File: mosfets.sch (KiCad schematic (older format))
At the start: 72 parts, among them P5 HP_MOSFETS, P6 MP_MOSFETS, Q1 2N7002P, Q10 2N7002P, Q11 2N7002P, Q12 BC846BPDW1, Q13 BC846BPDW1, Q14 SI2318CDS-T1-GE3, Q15 IRFB7545PbF, Q16 2N7002P, Q17 2N7002P, Q18 BC846BPDW1, Q19 BC846BPDW1, Q2 2N7002P, Q20 SI2318CDS-T1-GE3, Q21 IRFB7545PbF, Q3 2N7002P, Q4 BC846BPDW1, Q5 BC846BPDW1, Q6 BC846BPDW1, Q7 IRFB7545PbF, Q8 SI2318CDS-T1-GE3, Q9 IRFB7545PbF

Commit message: fixed minor issue
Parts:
- Q15, Q21, Q7, Q9: footprint to:TO-220 -> to:TO-220-3
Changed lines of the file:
@@
 F 0 "Q9" H 3302 1935 34  0000 L CNN
 F 1 "IRFB7545PbF" H 3302 1866 34  0000 L CNN
-F 2 "to:TO-220" H 2925 1700 60  0001 C CNN
+F 2 "to:TO-220-3" H 2925 1700 60  0001 C CNN
 F 3 "" H 2925 1700 60  0000 C CNN
 	1    2925 1700
@@
 F 0 "Q21" H 8677 1935 34  0000 L CNN
 F 1 "IRFB7545PbF" H 8677 1866 34  0000 L CNN
-F 2 "to:TO-220" H 8300 1700 60  0001 C CNN
+F 2 "to:TO-220-3" H 8300 1700 60  0001 C CNN
 F 3 "" H 8300 1700 60  0000 C CNN
 	1    8300 1700
@@
 F 0 "Q7" H 3252 5835 34  0000 L CNN
 F 1 "IRFB7545PbF" H 3252 5766 34  0000 L CNN
-F 2 "to:TO-220" H 2875 5600 60  0001 C CNN
+F 2 "to:TO-220-3" H 2875 5600 60  0001 C CNN
 F 3 "" H 2875 5600 60  0000 C CNN
 	1    2875 5600
@@
 F 0 "Q15" H 6052 1935 34  0000 L CNN
 F 1 "IRFB7545PbF" H 6052 1866 34  0000 L CNN
-F 2 "to:TO-220" H 5675 1700 60  0001 C CNN
+F 2 "to:TO-220-3" H 5675 1700 60  0001 C CNN
 F 3 "" H 5675 1700 60  0000 C CNN
 	1    5675 1700

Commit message: fixed some errors
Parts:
- D11, D15, D7: footprint diodes:SOD-80C -> diodes:DO213AA_SOD-80_MiniMelf
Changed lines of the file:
@@
 F 0 "D7" V 3298 3047 34  0000 R CNN
 F 1 "1n4148" V 3229 3047 34  0000 R CNN
-F 2 "diodes:SOD-80C" H 3150 3075 60  0001 C CNN
+F 2 "diodes:DO213AA_SOD-80_MiniMelf" H 3150 3075 60  0001 C CNN
 F 3 "" H 3150 3075 60  0000 C CNN
 	1    3150 3075
@@
 F 0 "D11" V 6048 3047 34  0000 R CNN
 F 1 "1n4148" V 5979 3047 34  0000 R CNN
-F 2 "diodes:SOD-80C" H 5900 3075 60  0001 C CNN
+F 2 "diodes:DO213AA_SOD-80_MiniMelf" H 5900 3075 60  0001 C CNN
 F 3 "" H 5900 3075 60  0000 C CNN
 	1    5900 3075
@@
 F 0 "D15" V 8673 3047 34  0000 R CNN
 F 1 "1n4148" V 8604 3047 34  0000 R CNN
-F 2 "diodes:SOD-80C" H 8525 3075 60  0001 C CNN
+F 2 "diodes:DO213AA_SOD-80_MiniMelf" H 8525 3075 60  0001 C CNN
 F 3 "" H 8525 3075 60  0000 C CNN
 	1    8525 3075

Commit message: - added wifi esp8266 - switched caps to smd - fixed dual transistor pinout bug
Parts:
- D11, D15, D7: symbol 1n4148 -> 1n4148-RESCUE-rados
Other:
- moved on the sheet: R10, R11, R12, R13, R14, R15, R16, R17, R18, R19, R20, R21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

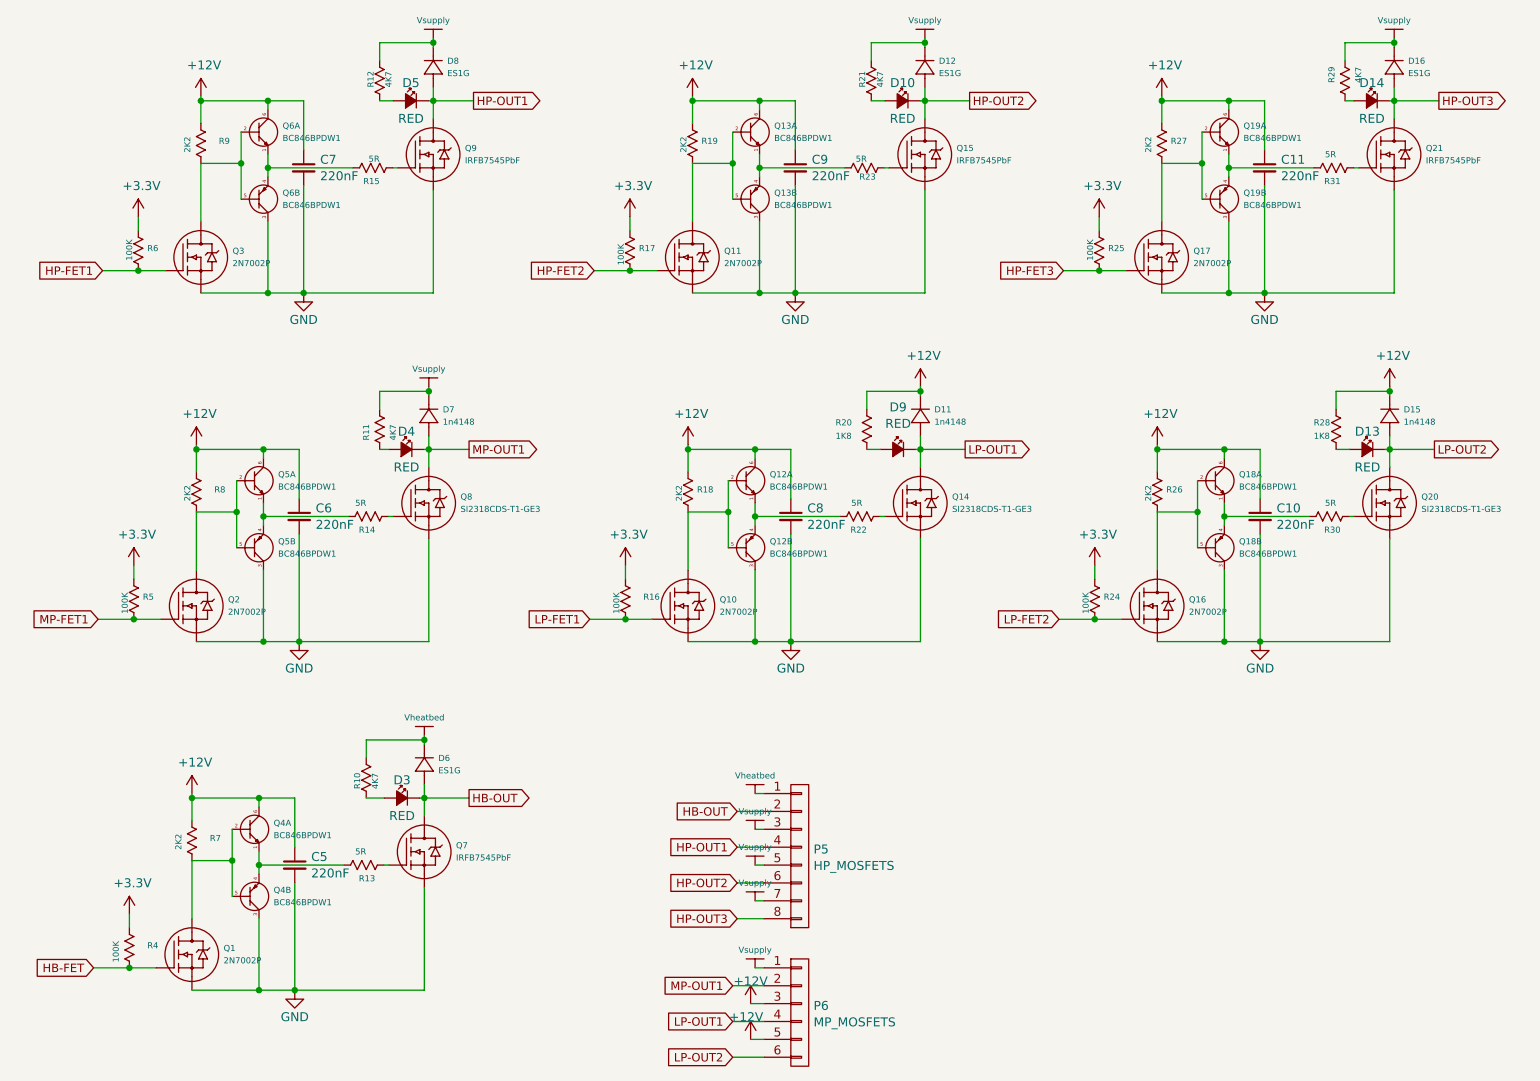
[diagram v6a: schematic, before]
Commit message: Changed gate resistor values
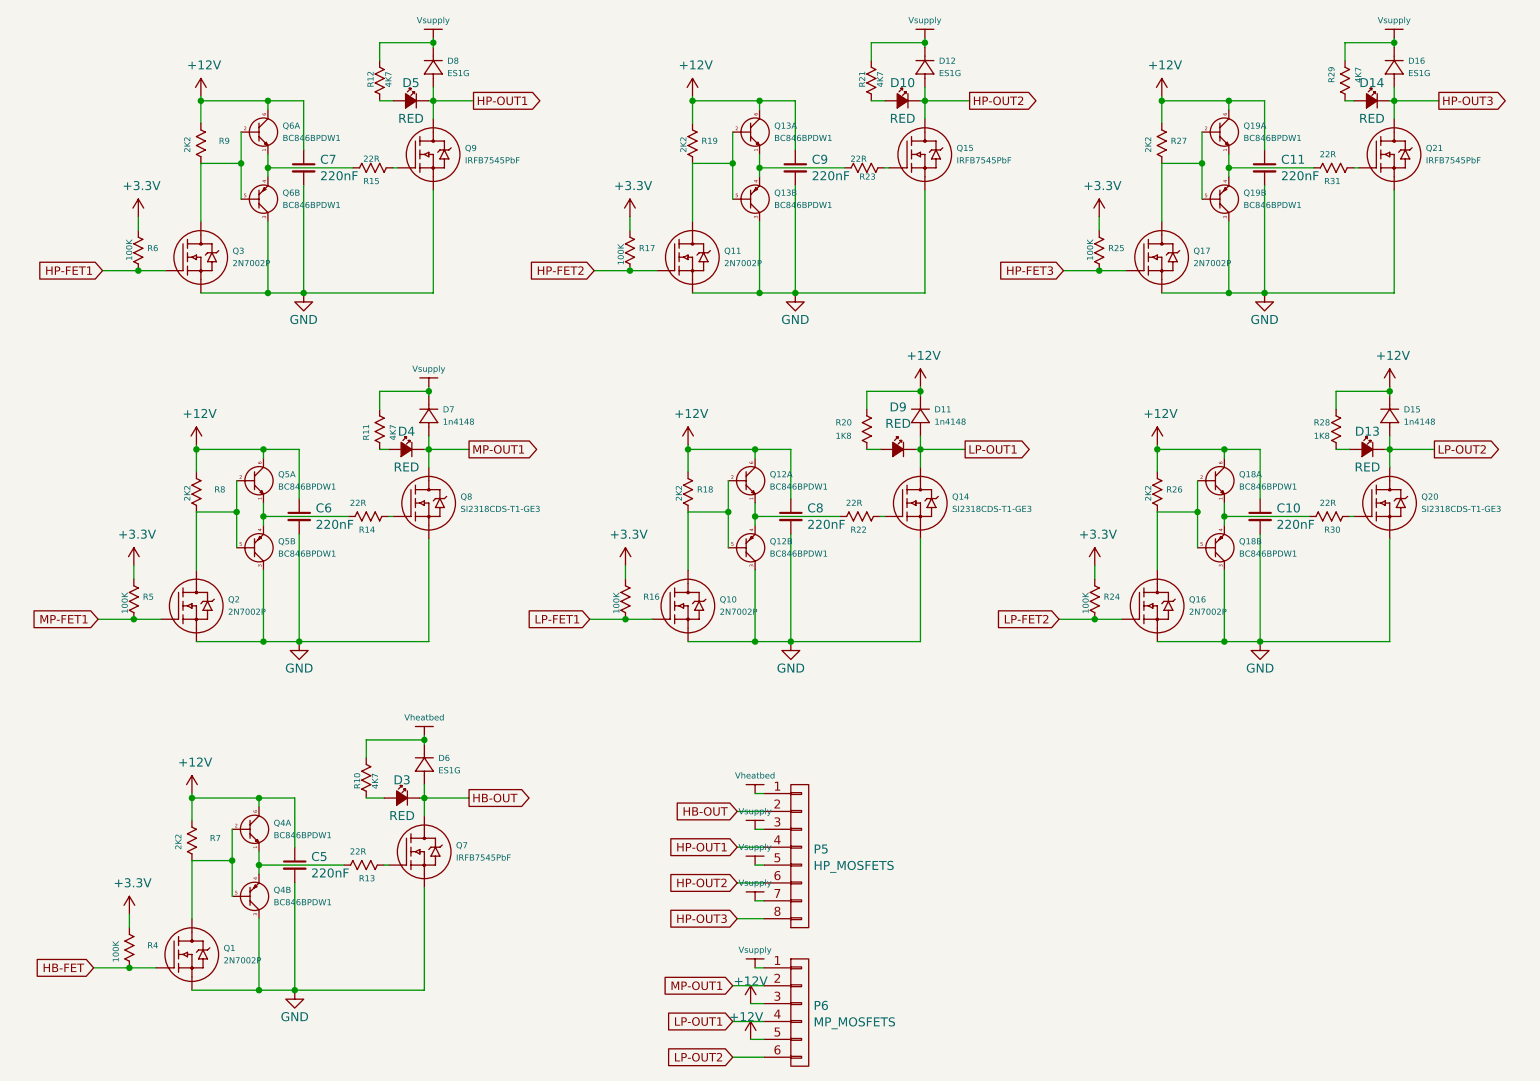
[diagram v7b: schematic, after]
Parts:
- R13, R14, R15, R22, R23, R30, R31: value 5R -> 22R
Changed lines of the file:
@@
 P 2675 1650
 F 0 "R15" H 2825 1650 34  0000 R CNN
-F 1 "5R" H 2825 1775 34  0000 R CNN
+F 1 "22R" H 2825 1775 34  0000 R CNN
 F 2 "resistors:R_0603" H 2675 1650 60  0001 C CNN
 F 3 "" H 2675 1650 60  0000 C CNN
@@
 P 8050 1650
 F 0 "R31" H 8200 1650 34  0000 R CNN
-F 1 "5R" H 8175 1800 34  0000 R CNN
+F 1 "22R" H 8175 1800 34  0000 R CNN
 F 2 "resistors:R_0603" H 8050 1650 60  0001 C CNN
 F 3 "" H 8050 1650 60  0000 C CNN
@@
 P 2625 5550
 F 0 "R13" H 2800 5550 34  0000 R CNN
-F 1 "5R" H 2750 5700 34  0000 R CNN
+F 1 "22R" H 2750 5700 34  0000 R CNN
 F 2 "resistors:R_0603" H 2625 5550 60  0001 C CNN
 F 3 "" H 2625 5550 60  0000 C CNN
@@
 P 2650 3600
 F 0 "R14" H 2800 3600 34  0000 R CNN
-F 1 "5R" H 2750 3750 34  0000 R CNN
+F 1 "22R" H 2750 3750 34  0000 R CNN
 F 2 "resistors:R_0603" H 2650 3600 60  0001 C CNN
 F 3 "" H 2650 3600 60  0000 C CNN
@@
 P 5400 3600
 F 0 "R22" H 5550 3600 34  0000 R CNN
-F 1 "5R" H 5525 3750 34  0000 R CNN
+F 1 "22R" H 5525 3750 34  0000 R CNN
 F 2 "resistors:R_0603" H 5400 3600 60  0001 C CNN
 F 3 "" H 5400 3600 60  0000 C CNN
@@
 P 8025 3600
 F 0 "R30" H 8200 3600 34  0000 R CNN
-F 1 "5R" H 8175 3750 34  0000 R CNN
+F 1 "22R" H 8175 3750 34  0000 R CNN
 F 2 "resistors:R_0603" H 8025 3600 60  0001 C CNN
 F 3 "" H 8025 3600 60  0000 C CNN
@@
 P 5425 1650
 F 0 "R23" H 5600 1675 34  0000 R CNN
-F 1 "5R" H 5550 1775 34  0000 R CNN
+F 1 "22R" H 5550 1775 34  0000 R CNN
 F 2 "resistors:R_0603" H 5425 1650 60  0001 C CNN
 F 3 "" H 5425 1650 60  0000 C CNN

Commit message: Added component specifications
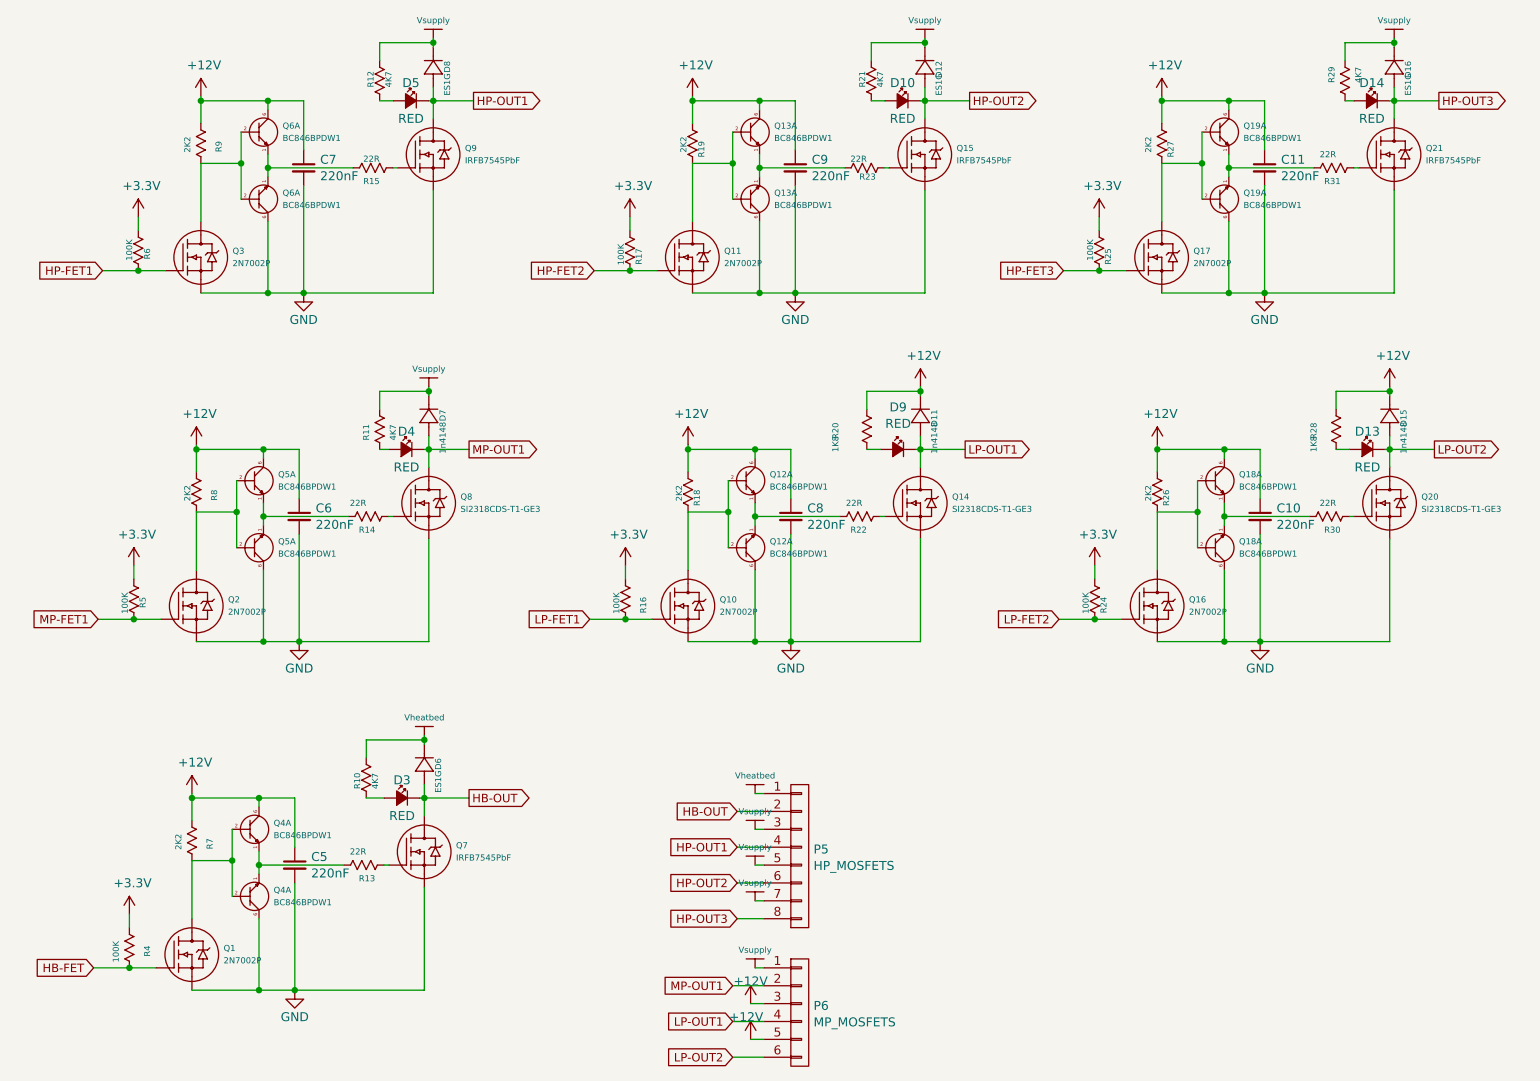
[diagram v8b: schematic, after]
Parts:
- C10, C11, C5, C6, C7, C8, C9: Specification (none) -> X7R
- D12, D16, D6, D8: Manufacturer (none) -> Fairchild Semiconductor; ManufacturerNo (none) -> ES1G
- Q1, Q10, Q11, Q16, Q17, Q2, Q3: Manufacturer (none) -> On Semiconductor; ManufacturerNo (none) -> 2N7002ET1G
- Q12, Q13, Q18, Q19, Q4, Q5, Q6: Manufacturer (none) -> On Semiconductor; ManufacturerNo (none) -> BC846BPDW1T1G
- Q14, Q20, Q8: Manufacturer (none) -> Vishay; ManufacturerNo (none) -> SI2318CDS-T1-GE3
- Q15, Q21, Q7, Q9: Manufacturer (none) -> International Rectifier; ManufacturerNo (none) -> IRFB7545PbF
- R10, R11, R12, R21, R29: Specification (none) -> 1%
- R13, R14, R15, R16, R17, R18, R19, R20, R22, R23, R24, R25, R26, R27, R28, R30, R31, R4, R5, R6, R7, R8, R9: Specification (none) -> 5%
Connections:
- net GND: now also Q12.6 (C), Q13.6 (C), Q18.6 (C), Q19.6 (C), Q4.6 (C), Q5.6 (C), Q6.6 (C); no longer Q12.3 (C), Q13.3 (C), Q18.3 (C), Q19.3 (C), Q4.3 (C), Q5.3 (C), Q6.3 (C)
- net at Q3.3 (D), Q6.2 (B), R9.1: now also Q6.2 (B); no longer Q6.5 (B)
- net at Q6.1 (E), R15.1: now also Q6.1 (E); no longer Q6.4 (E)
- net at Q11.3 (D), Q13.2 (B), R19.1: now also Q13.2 (B); no longer Q13.5 (B)
- net at Q13.1 (E), R23.1: now also Q13.1 (E); no longer Q13.4 (E)
- net at Q17.3 (D), Q19.2 (B), R27.1: now also Q19.2 (B); no longer Q19.5 (B)
- net at Q19.1 (E), R31.1: now also Q19.1 (E); no longer Q19.4 (E)
- net at Q1.3 (D), Q4.2 (B), R7.1: now also Q4.2 (B); no longer Q4.5 (B)
- net at Q4.1 (E), R13.1: now also Q4.1 (E); no longer Q4.4 (E)
- net at Q2.3 (D), Q5.2 (B), R8.1: now also Q5.2 (B); no longer Q5.5 (B)
- net at Q5.1 (E), R14.1: now also Q5.1 (E); no longer Q5.4 (E)
- net at Q10.3 (D), Q12.2 (B), R18.1: now also Q12.2 (B); no longer Q12.5 (B)
- net at Q12.1 (E), R22.1: now also Q12.1 (E); no longer Q12.4 (E)
- net at Q16.3 (D), Q18.2 (B), R26.1: now also Q18.2 (B); no longer Q18.5 (B)
- net at Q18.1 (E), R30.1: now also Q18.1 (E); no longer Q18.4 (E)
